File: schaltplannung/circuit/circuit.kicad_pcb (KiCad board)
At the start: 2 copper layers, 116 x 91 mm, 7 parts, among them J1 Conn_01x04_Pin, J2 Conn_01x08_Pin, SW1 SW_Push, SW2 SW_Push, U1 DHT11, U2 XIAO-ESP32-C3-SMD

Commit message: added images and exported gerber files
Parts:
- added G***: LOGO, LOGO, F.Cu at (157.0, 100.0)
- added G***: LOGO, LOGO, F.Cu at (129.6, 115.0)
- added G***: LOGO, LOGO, F.Cu at (180.0, 110.0)

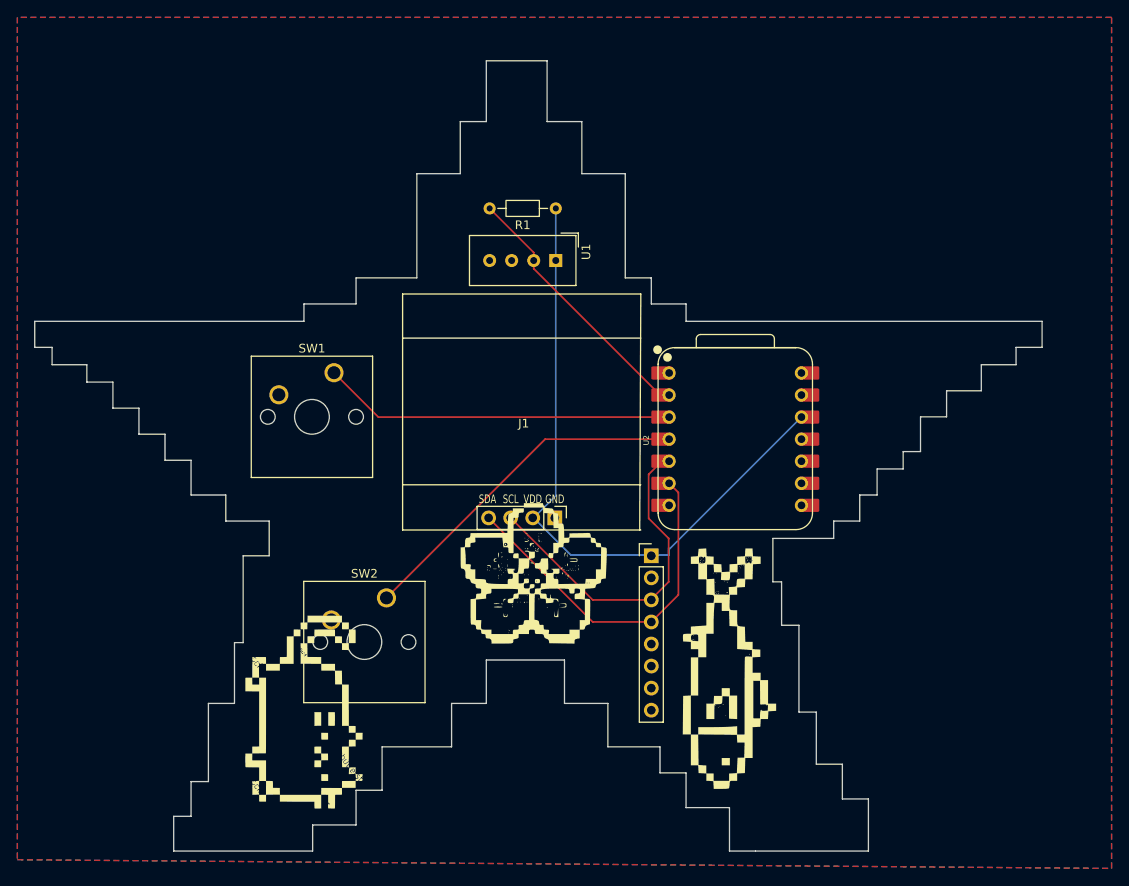
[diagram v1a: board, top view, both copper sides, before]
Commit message: made the PCB smaller to minimize the costs
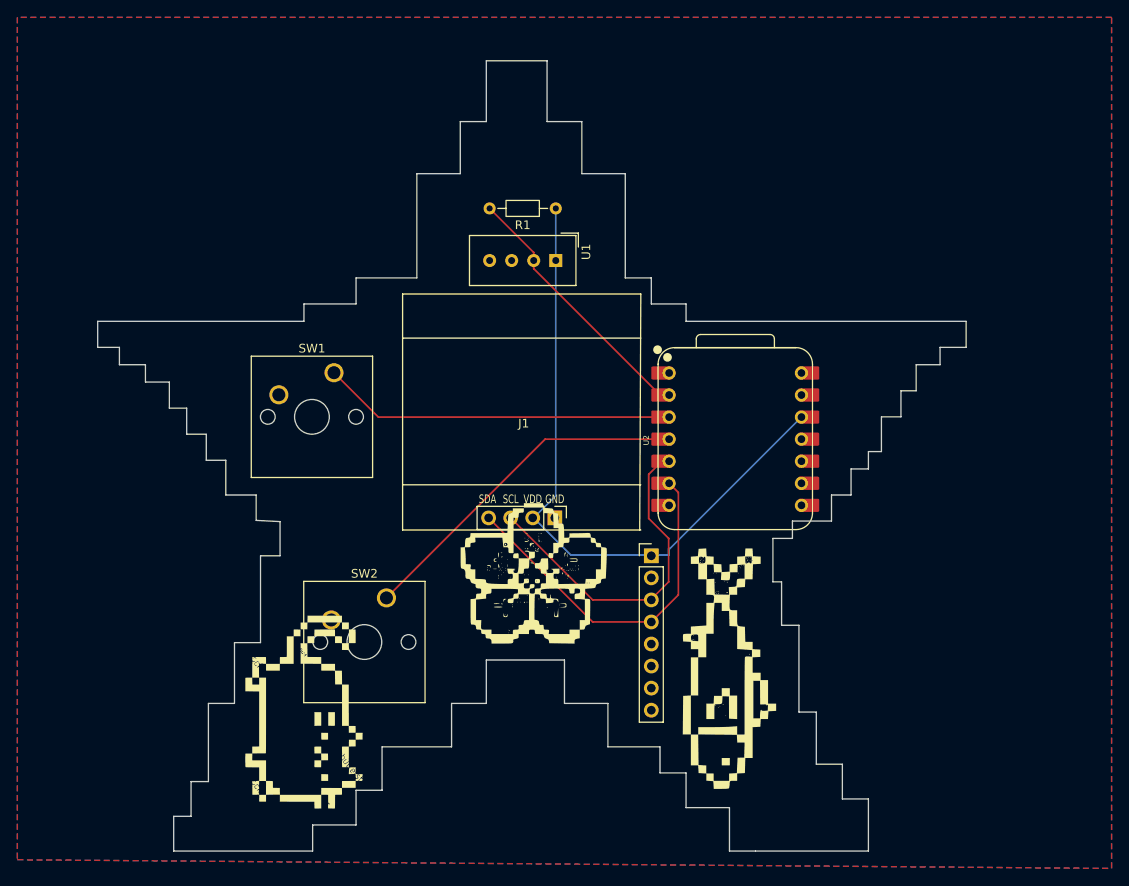
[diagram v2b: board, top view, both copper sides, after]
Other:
- board size 116 x 91 mm -> 100 x 91 mm
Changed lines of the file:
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@@
 		(pts
 			(xy 152 40) (xy 159 40) (xy 159 47) (xy 163 47) (xy 163 53) (xy 168 53) (xy 168 65) (xy 171 65) (xy 171 68)
-			(xy 175 68) (xy 175 70) (xy 216 70) (xy 216 73) (xy 213 73) (xy 213 75) (xy 209 75) (xy 209 78) (xy 205 78)
-			(xy 205 81) (xy 202 81) (xy 202 85) (xy 200 85) (xy 200 87) (xy 197 87) (xy 197 90) (xy 195 90) (xy 195 93)
-			(xy 192 93) (xy 192 95) (xy 185 95) (xy 185 100) (xy 186 100) (xy 186 105) (xy 188 105) (xy 188 115)
-			(xy 190 115) (xy 190 121) (xy 193 121) (xy 193 125) (xy 196 125) (xy 196 131) (xy 183 131) (xy 180 131)
-			(xy 180 126) (xy 175 126) (xy 175 122) (xy 172 122) (xy 172 119) (xy 166 119) (xy 166 114) (xy 161 114)
-			(xy 161 109) (xy 152 109) (xy 152 114) (xy 148 114) (xy 148 119) (xy 140 119) (xy 140 124) (xy 137 124)
-			(xy 137 128) (xy 132 128) (xy 132 131) (xy 116 131) (xy 116 127) (xy 118 127) (xy 118 123) (xy 120 123)
-			(xy 120 114) (xy 123 114) (xy 123 107) (xy 124 107) (xy 124 97) (xy 127 97) (xy 127 93) (xy 122 93)
-			(xy 122 90) (xy 118 90) (xy 118 86) (xy 115 86) (xy 115 83) (xy 112 83) (xy 112 80) (xy 109 80) (xy 109 77)
-			(xy 106 77) (xy 106 75) (xy 102 75) (xy 102 73) (xy 100 73) (xy 100 70) (xy 131 70) (xy 131 68) (xy 137 68)
-			(xy 137 65) (xy 144 65) (xy 144 53) (xy 149 53) (xy 149 47) (xy 152 47)
+			(xy 175 68) (xy 175 70) (xy 207.25 70) (xy 207.25 73) (xy 204.25 73) (xy 204.25 75) (xy 201.5 75)
+			(xy 201.5 78) (xy 199.75 78) (xy 199.75 81) (xy 197.5 81) (xy 197.5 85) (xy 196 85) (xy 196 87) (xy 194 87)
+			(xy 194 90) (xy 191.75 90) (xy 191.75 93) (xy 187.25 93) (xy 187.25 95) (xy 185 95) (xy 185 100)
+			(xy 186 100) (xy 186 105) (xy 188 105) (xy 188 115) (xy 190 115) (xy 190 121) (xy 193 121) (xy 193 125)
+			(xy 196 125) (xy 196 131) (xy 183 131) (xy 180 131) (xy 180 126) (xy 175 126) (xy 175 122) (xy 172 122)
+			(xy 172 119) (xy 166 119) (xy 166 114) (xy 161 114) (xy 161 109) (xy 152 109) (xy 152 114) (xy 148 114)
+			(xy 148 119) (xy 140 119) (xy 140 124) (xy 137 124) (xy 137 128) (xy 132 128) (xy 132 131) (xy 116 131)
+			(xy 116 127) (xy 118 127) (xy 118 123) (xy 120 123) (xy 120 114) (xy 123 114) (xy 123 107) (xy 126 107)
+			(xy 126 97) (xy 128.25 97) (xy 128.25 93.0625) (xy 125.5 92.925) (xy 125.5 90) (xy 122 90) (xy 122 86)
+			(xy 119.75 86) (xy 119.75 83) (xy 117.5 83) (xy 117.5 80) (xy 115.5 80) (xy 115.5 77) (xy 112.75 77)
+			(xy 112.75 75) (xy 109.75 75) (xy 109.75 73) (xy 107.25 73) (xy 107.25 70) (xy 131 70) (xy 131 68)
+			(xy 137 68) (xy 137 65) (xy 144 65) (xy 144 53) (xy 149 53) (xy 149 47) (xy 152 47)
 		)
 		(stroke
